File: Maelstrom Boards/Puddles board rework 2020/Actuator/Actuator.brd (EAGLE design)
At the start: 101.6 x 101.6 mm, 75 parts, among them Y1 12MHz, Y3 32.768kHz

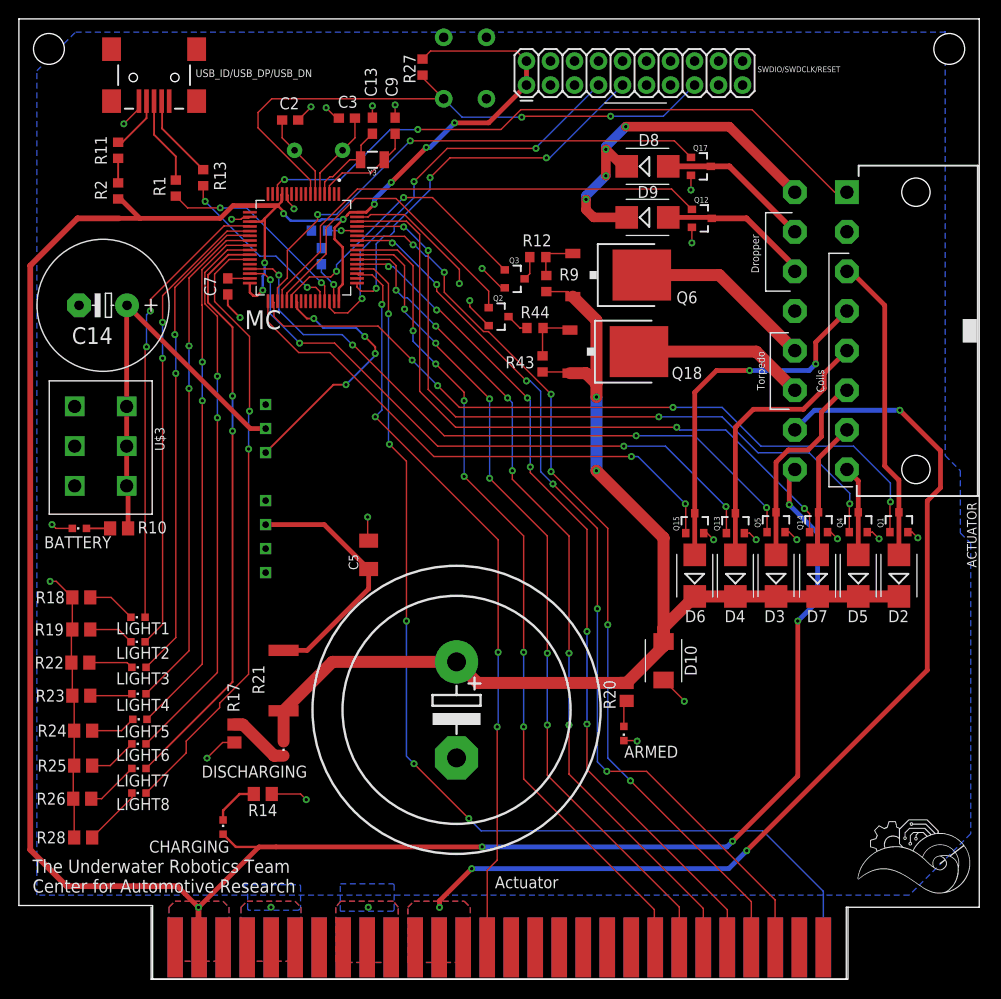
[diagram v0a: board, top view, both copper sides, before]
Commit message: Puddles board rework 2020: Battery Balancer and Actuator
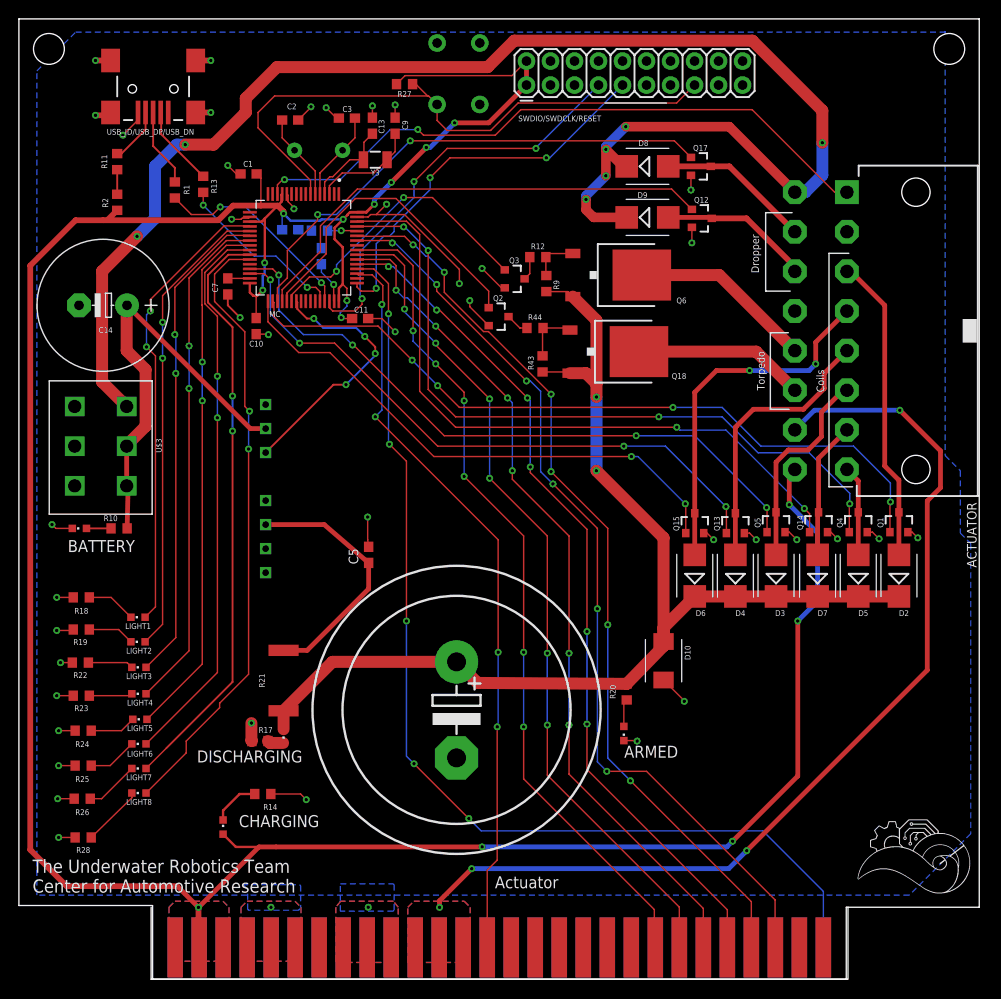
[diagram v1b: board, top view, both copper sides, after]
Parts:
- added C1, C6: 0.1uF, rcl:C0603
- added C10, C11: 1uF, rcl:C0603
- C5: device resistor:C1206K -> rcl:C0603
- R10, R14, R17, R18, R19, R20, R22, R23, R24, R25, R26, R28: device resistor:R0805 -> rcl:R0603
- moved R17 2.82 mm to (25.5, 25.2), turned to 0 degrees
- moved R27 2.62 mm to (40.8, 94.7), turned to 180 degrees
- moved DISCHARGING 1.30 mm to (28.0, 25.7)
- moved USB_ID/USB_DP/USB_DN 1.20 mm to (14.2, 94.2)
- moved R11 1.20 mm to (10.4, 86.5)
- moved R2 1.20 mm to (10.4, 82.2)
- moved RESET_SWITCH 0.92 mm to (46.5, 95.8)
- moved R13 0.70 mm to (19.5, 84.1)
- moved Y3 0.30 mm to (37.7, 86.7)
- moved R1 0.22 mm to (16.5, 83.5)
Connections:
- net +12V: now also U$3.1+
- net +3V3: now also C1.1, C10.1, C11.1, C6.1
- net AGND: now also C1.2, C10.2, C11.2, C6.2, USB_ID/USB_DP/USB_DN.S1, USB_ID/USB_DP/USB_DN.S2, USB_ID/USB_DP/USB_DN.S3, USB_ID/USB_DP/USB_DN.S4
- net V+: no longer U$3.1+
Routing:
- net +12V: track 38.9 -> 158.2 mm, vias 4 -> 7
- net +3V3: track 301.2 -> 315.9 mm, vias 13 -> 15
- net N$15: track 6.57 -> 1.75 mm
- net V+: track 43.7 -> 45.4 mm
- net AGND: track 95.4 -> 93.8 mm, vias 28 -> 43
- net +24V: track 126.1 -> 124.8 mm
- net RESET: track 63.4 -> 64.4 mm, vias 2 -> 0
- net N$7: track 9.30 -> 8.30 mm
- net LED1: track 47.6 -> 48.4 mm
- net USB_DP: track 21.3 -> 22.0 mm
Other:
- board text added: "3.3V"
- board text added: "GND"
- board text added: "RESET"
- board text added: "SWCLK"
- board text added: "SWDIO"

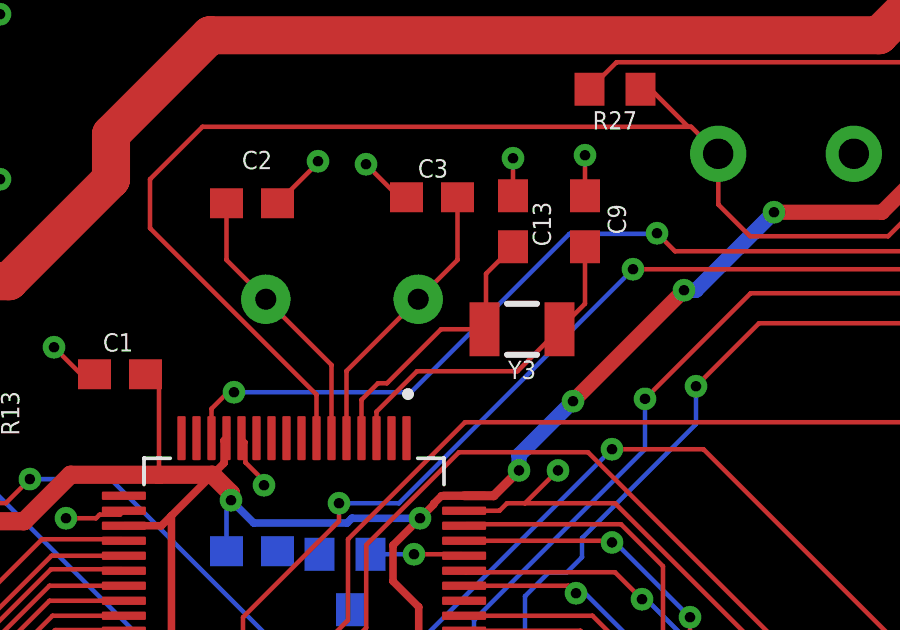
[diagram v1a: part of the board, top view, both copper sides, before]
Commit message: final commit for ESC board, resistor values changed across boards for order ease
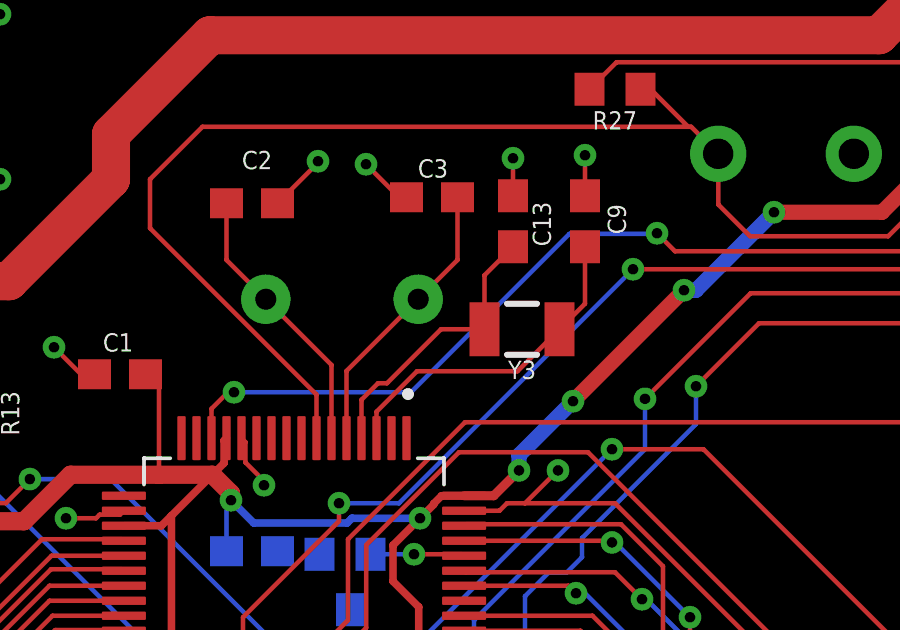
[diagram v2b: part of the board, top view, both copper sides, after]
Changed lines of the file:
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@@
 <contactref element="Y3" pad="P$1"/>
 <contactref element="C13" pad="1"/>
-<wire x1="36.1" y1="86.7" x2="35" y2="86.7" width="0.1524" layer="1"/>
 <wire x1="33.2" y1="84.9" x2="32.9" y2="84.9" width="0.1524" layer="1"/>
 <wire x1="32.9" y1="84.9" x2="32.35" y2="84.35" width="0.1524" layer="1"/>
 <wire x1="32.35" y1="84.35" x2="32.35" y2="83.07" width="0.1524" layer="1"/>
-<wire x1="35" y1="86.7" x2="33.2" y2="84.9" width="0.1524" layer="1"/>
-<wire x1="37.4" y1="89.45" x2="36.5" y2="88.55" width="0.1524" layer="1"/>
-<wire x1="36.2" y1="86.8" x2="36.1" y2="86.7" width="0.1524" layer="1"/>
-<wire x1="36.5" y1="88.55" x2="36.5" y2="86.75" width="0.1524" layer="1"/>
-<wire x1="36.45" y1="86.7" x2="36.5" y2="86.75" width="0.1524" layer="1"/>
+<wire x1="33.2" y1="84.9" x2="35" y2="86.7" width="0.1524" layer="1"/>
+<wire x1="35" y1="86.7" x2="36.45" y2="86.7" width="0.1524" layer="1"/>
+<wire x1="36.45" y1="88.5" x2="36.45" y2="86.7" width="0.1524" layer="1"/>
+<wire x1="37.4" y1="89.45" x2="36.45" y2="88.5" width="0.1524" layer="1"/>
 </signal>
 <signal name="N$29">

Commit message: updates to puddles board rework actuator and BB.
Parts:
- removed C14: 1000 uF, rcl:E5-13
- removed CHARGING: (no value), led:CHIPLED_0603
- removed R14: 100, rcl:R0603
- LIGHT1, LIGHT2, LIGHT3, LIGHT4, LIGHT5, LIGHT6, LIGHT7, LIGHT8: value (none) -> Red
- moved R17 7.82 mm to (28.3, 17.9), turned to 90 degrees
- moved DISCHARGING 4.21 mm to (28.3, 21.5)
- moved LIGHT1 3.02 mm to (10.1, 40.0)
- moved LIGHT2 2.95 mm to (10.0, 37.1)
- moved LIGHT3 2.35 mm to (10.4, 33.5)
- moved LIGHT5 2.30 mm to (10.5, 27.5)
- moved LIGHT4 2.30 mm to (10.4, 30.2)
- moved LIGHT6 2.30 mm to (10.4, 24.9)
- moved LIGHT7 2.30 mm to (10.4, 22.3)
- moved LIGHT8 2.30 mm to (10.4, 19.7)
- moved R18 0.41 mm to (6.50, 40.0)
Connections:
- removed net N$4: CHARGING.C, R14.2
- net +3V3: no longer CHARGING.A
- net AGND: no longer C14.-, R14.1
- net V+: no longer C14.+
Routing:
- net V+: track 45.4 -> 24.2 mm
- net +3V3: track 315.9 -> 309.7 mm
- net N$4: track 5.07 -> 0.00 mm
- net AGND: track 93.8 -> 89.4 mm, vias 43 -> 42
- net +24V: track 124.8 -> 129.2 mm
- net N$16: track 5.27 -> 2.00 mm
- net N$17: track 4.94 -> 1.84 mm
- net N$18: track 4.81 -> 2.30 mm
- net N$21: track 4.90 -> 2.60 mm
- net N$19: track 4.58 -> 2.28 mm
- net N$22: track 5.25 -> 3.13 mm
- net N$23: track 5.73 -> 4.07 mm
- net LED1: track 48.4 -> 46.9 mm, vias 2 -> 0
- net LED7: track 62.4 -> 63.6 mm, vias 2 -> 0
- net LED8: track 65.3 -> 66.5 mm, vias 2 -> 0
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
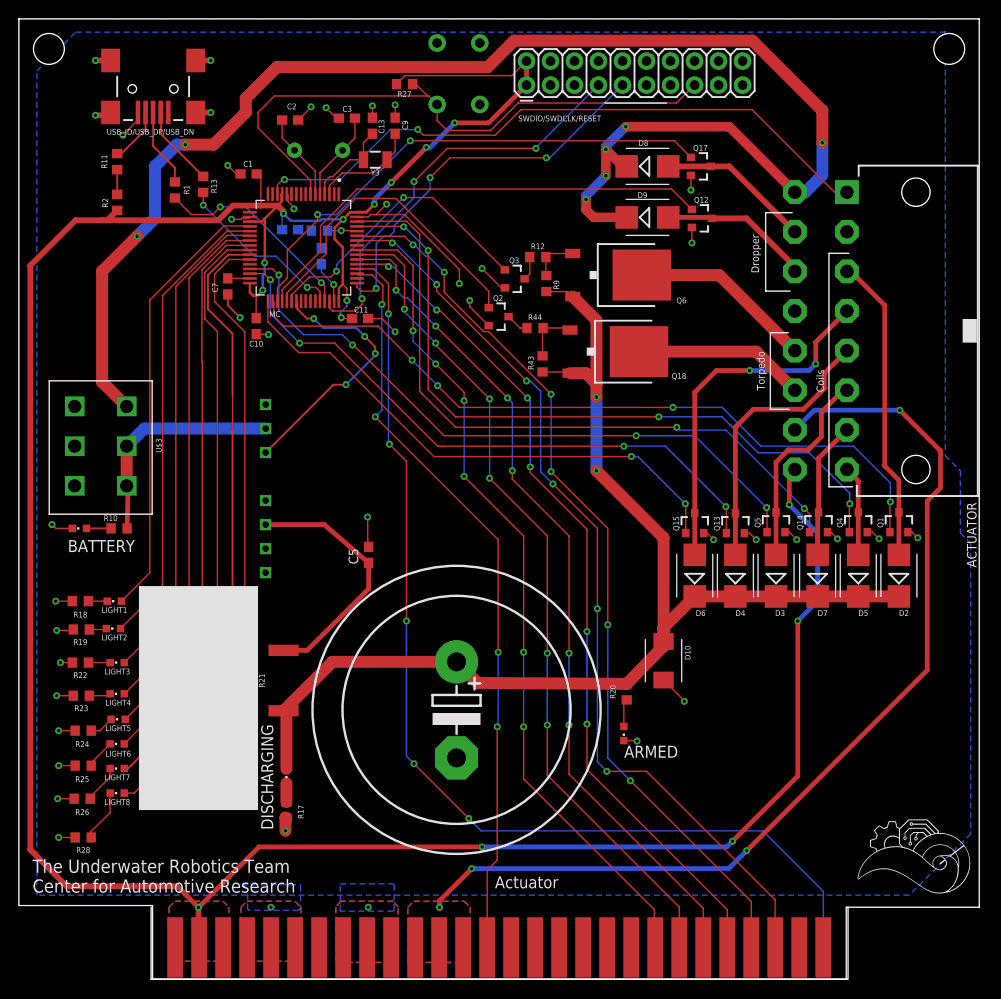
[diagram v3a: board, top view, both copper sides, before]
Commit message: updates to puddles acutator board. Resistor wattage concerns addressed
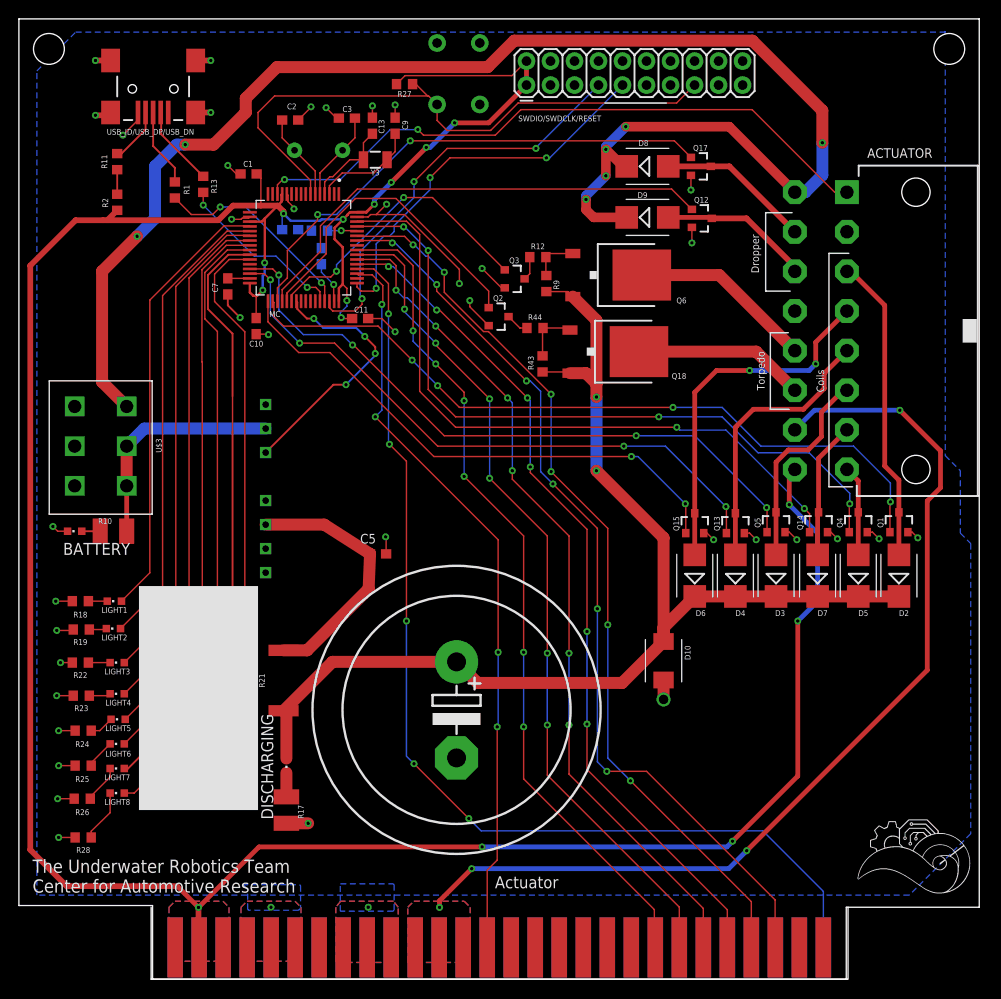
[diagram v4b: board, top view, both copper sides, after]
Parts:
- removed ARMED: (no value), led:CHIPLED_0603
- removed R20: 1.2k, rcl:R0603
- DISCHARGING: value (none) -> Green
- R10: device rcl:R0603 -> rcl:R1210
- R17: value 1.5k -> 1K; device rcl:R0603 -> rcl:R1210
- moved DISCHARGING 1.10 mm to (28.3, 22.6)
- moved C5 1.00 mm to (38.0, 45.0), turned to 0 degrees
- moved R10 0.67 mm to (10.0, 47.4)
- moved BATTERY 0.58 mm to (5.90, 47.4)
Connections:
- removed net N$10: ARMED.A, R20.1
- net +24V: no longer R20.2
- net AGND: no longer ARMED.C
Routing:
- net AGND: track 89.4 -> 85.8 mm, vias 42 -> 41
- net N$10: track 2.90 -> 0.00 mm
- net +24V: track 129.2 -> 127.7 mm
- net N$9: track 2.60 -> 1.95 mm
- net N$15: track 2.00 -> 2.55 mm
- net N$26: track 26.8 -> 27.4 mm

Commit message: Changing puddles actuator crystal caps
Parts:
- C13, C9: value 12.5pF -> 18pF
- C2, C3: value 18pF -> 30pF
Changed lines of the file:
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@@
 <?xml version="1.0" encoding="utf-8"?>
 <!DOCTYPE eagle SYSTEM "eagle.dtd">
-<eagle version="9.5.2">
+<eagle version="9.6.2">
 <drawing>
 <settings>
@@
 <attribute name="SF_ID" value="COM-00536" x="-0.4" y="67" size="1.778" layer="28" rot="MR180" display="off"/>
 </element>
-<element name="C2" library="rcl" library_urn="urn:adsk.eagle:library:334" package="C0603" package3d_urn="urn:adsk.eagle:package:23616/2" value="18pF" x="28.7" y="90.9" smashed="yes">
+<element name="C2" library="rcl" library_urn="urn:adsk.eagle:library:334" package="C0603" package3d_urn="urn:adsk.eagle:package:23616/2" value="30pF" x="28.7" y="90.9" smashed="yes">
 <attribute name="NAME" x="28.365" y="92.035" size="0.6096" layer="25"/>
 <attribute name="POPULARITY" value="73" x="28.7" y="90.9" size="1.778" layer="27" display="off"/>
 <attribute name="SPICEPREFIX" value="C" x="-12.3" y="113" size="1.778" layer="27" display="off"/>
 </element>
-<element name="C3" library="rcl" library_urn="urn:adsk.eagle:library:334" package="C0603" package3d_urn="urn:adsk.eagle:package:23616/2" value="18pF" x="34.7" y="91.1" smashed="yes" rot="R180">
+<element name="C3" library="rcl" library_urn="urn:adsk.eagle:library:334" package="C0603" package3d_urn="urn:adsk.eagle:package:23616/2" value="30pF" x="34.7" y="91.1" smashed="yes" rot="R180">
 <attribute name="NAME" x="35.235" y="92.365" size="0.6096" layer="25" rot="R180"/>
 <attribute name="POPULARITY" value="73" x="34.7" y="91.1" size="1.778" layer="27" rot="R180" display="off"/>
@@
 <attribute name="PROD_ID" value="XTAL-13062" x="-1.4" y="89.7" size="1.778" layer="27" display="off"/>
 </element>
-<element name="C13" library="rcl" library_urn="urn:adsk.eagle:library:334" package="C0603" package3d_urn="urn:adsk.eagle:package:23616/2" value="12.5pF" x="37.4" y="90.3" smashed="yes" rot="R90">
+<element name="C13" library="rcl" library_urn="urn:adsk.eagle:library:334" package="C0603" package3d_urn="urn:adsk.eagle:package:23616/2" value="18pF" x="37.4" y="90.3" smashed="yes" rot="R90">
 <attribute name="NAME" x="38.665" y="89.465" size="0.6096" layer="25" rot="R90"/>
 <attribute name="POPULARITY" value="73" x="37.4" y="90.3" size="1.778" layer="27" rot="R90" display="off"/>
 <attribute name="SPICEPREFIX" value="C" x="43.2" y="59.9" size="1.778" layer="27" rot="R90" display="off"/>
 </element>
-<element name="C9" library="rcl" library_urn="urn:adsk.eagle:library:334" package="C0603" package3d_urn="urn:adsk.eagle:package:23616/2" value="12.5pF" x="39.8" y="90.3" smashed="yes" rot="R90">
+<element name="C9" library="rcl" library_urn="urn:adsk.eagle:library:334" package="C0603" package3d_urn="urn:adsk.eagle:package:23616/2" value="18pF" x="39.8" y="90.3" smashed="yes" rot="R90">
 <attribute name="NAME" x="41.165" y="89.865" size="0.6096" layer="25" rot="R90"/>
 <attribute name="POPULARITY" value="73" x="39.8" y="90.3" size="1.778" layer="27" rot="R90" display="off"/>
